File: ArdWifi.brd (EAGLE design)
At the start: 17.8 x 33 mm, 17 parts, among them Q1 8/16/20MHz, U1 ATMEGA328, U2 MIC5205

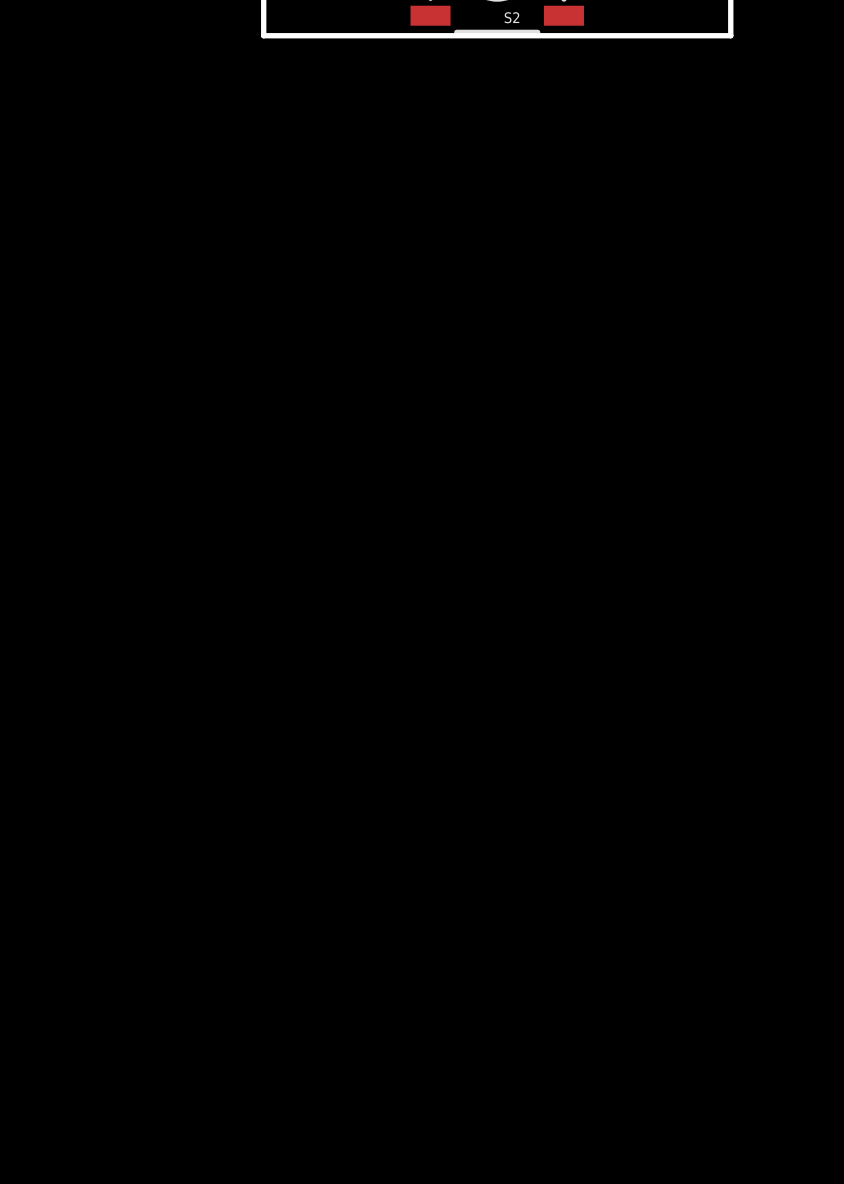
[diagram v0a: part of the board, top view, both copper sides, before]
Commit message: add wifi chip
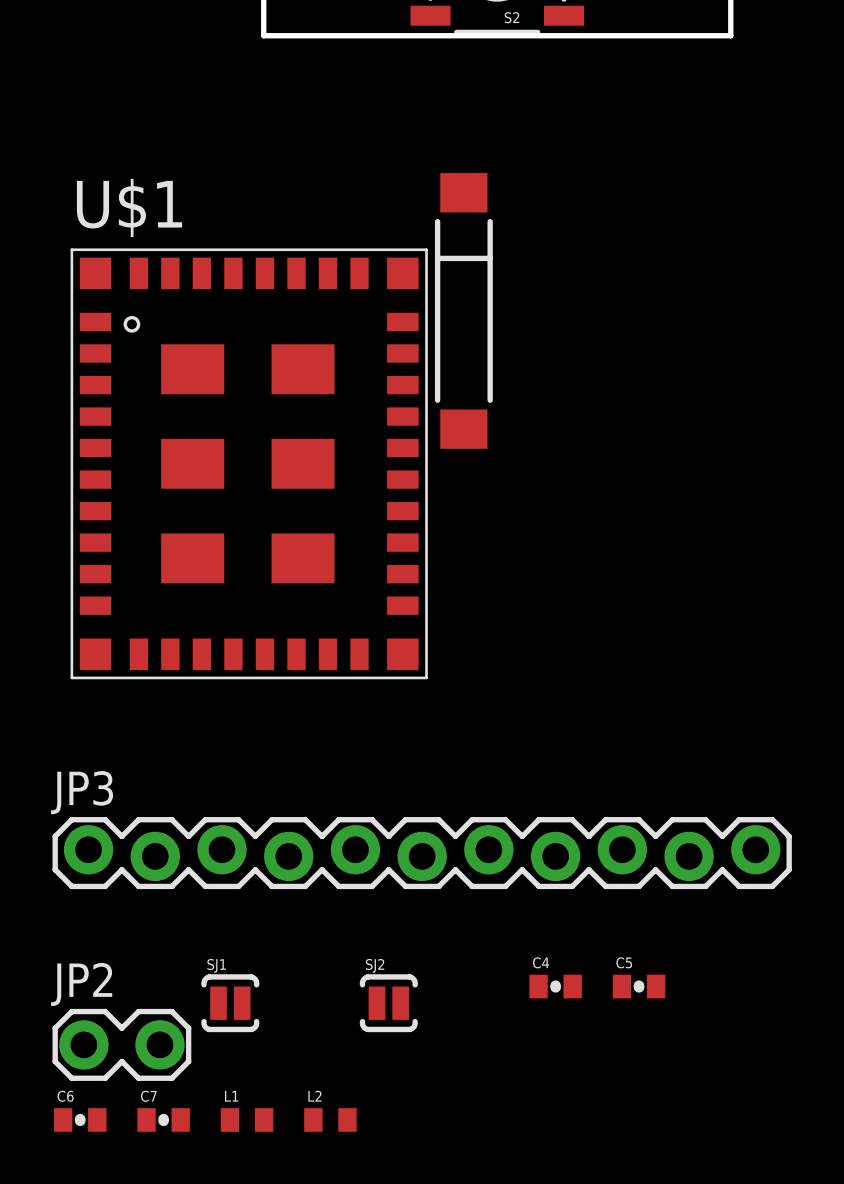
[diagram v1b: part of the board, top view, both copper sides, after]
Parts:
- added C4, C5: 1uF, SparkFun:0402-CAP
- added C6: 10pF, SparkFun:0402-CAP
- added C7: 2.2pF, SparkFun:0402-CAP
- added JP2: (no value), SparkFun:1X02_LOCK
- added JP3: M11LOCK, SparkFun:1X11_LOCK
- added L1: NL, SparkFun:C0402
- added L2: 2.2nH, SparkFun:C0402
- added SJ1, SJ2: SOLDERJUMPERNO, SparkFun:SJ_2S-NO
- added U$1: CC3000, centerblack_engineering:CC3000
- added U$3: ANTENNA2SMD2, SparkFun:ANTENNA-CHIP3
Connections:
- new net 3.3V: C5.2, JP3.11, U$1.P$19
- new net N$10: C6.1, C7.2, L2.2
- new net N$13: C6.2, U$1.P$35
- new net N$14: SJ1.1, U$1.P$30
- new net N$15: C7.1, L1.2, U$3.FEED
- new net N$16: SJ1.2, U$1.P$29
- new net N$17: SJ2.2, U$1.P$28
- new net N$18: SJ2.1, U$1.P$27
- new net SPI_CLK: JP3.7, U$1.P$17
- new net SPI_CS: JP3.3, U$1.P$12
- new net SPI_DIN: JP3.6, U$1.P$15
- new net SPI_DOUT: JP3.4, U$1.P$13
- new net SPI_IRQ: JP3.5, U$1.P$14
- new net VBAT_SW_EN: JP3.9, U$1.P$26
- new net VIO_HOST: C4.2, JP3.8, U$1.P$23
- new net WL_EN1: JP2.1, U$1.P$7
- new net WL_EN2: JP2.2, U$1.P$5
- new net WL_RS232_RX: JP3.2, U$1.P$8
- new net WL_RS232_TX: JP3.1, U$1.P$6
- net GND: now also C4.1, C5.1, JP3.10, L1.1, L2.1, U$1.P$1, U$1.P$10, U$1.P$11, U$1.P$16, U$1.P$18, U$1.P$20, U$1.P$21, U$1.P$22, U$1.P$25, U$1.P$31, U$1.P$32, U$1.P$33, U$1.P$34, U$1.P$36, U$1.P$37, U$1.P$38, U$1.P$39, U$1.P$40, U$1.P$41, U$1.P$42, U$1.P$43, U$1.P$44, U$1.P$45, U$1.P$46, U$1.P$9

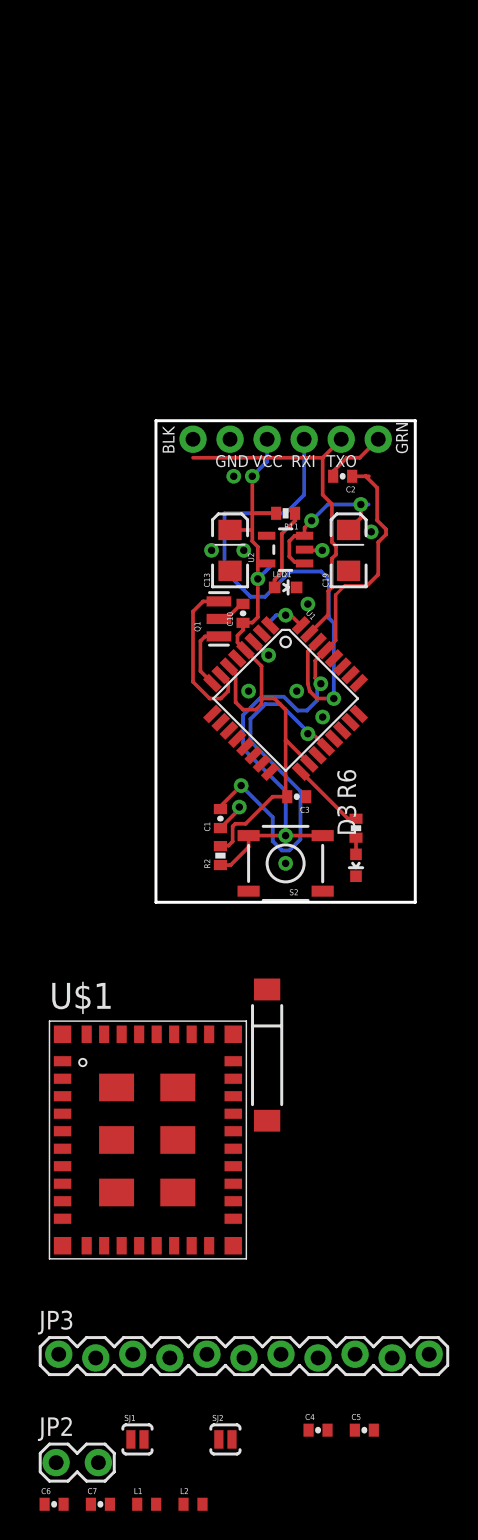
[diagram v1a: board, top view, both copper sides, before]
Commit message: connect wifi chip
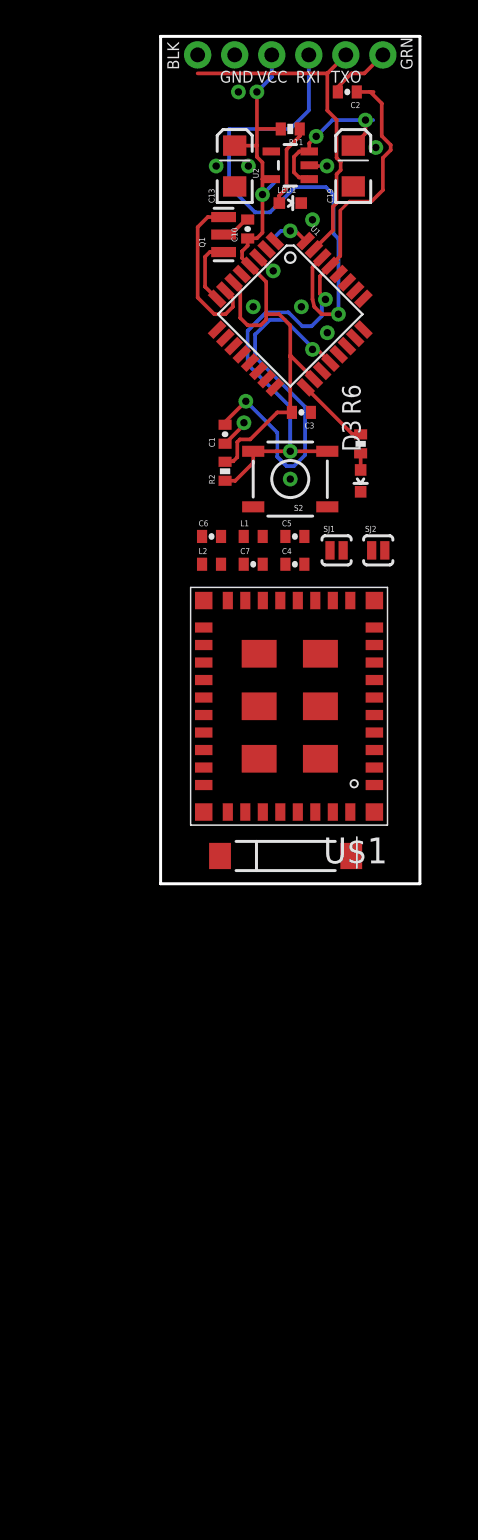
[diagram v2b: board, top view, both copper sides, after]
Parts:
- removed JP2: (no value), SparkFun:1X02_LOCK
- removed JP3: M11LOCK, SparkFun:1X11_LOCK
- moved C6 67.2 mm to (3.81, 25.1)
- moved L1 66.8 mm to (6.67, 25.1)
- moved C7 65.3 mm to (6.67, 23.2)
- moved L2 64.5 mm to (3.81, 23.2)
- moved SJ1 62.5 mm to (12.4, 24.1)
- moved SJ2 61.9 mm to (15.2, 24.1)
- moved C5 61.5 mm to (9.53, 25.1)
- moved C4 59.4 mm to (9.53, 23.2)
- moved U$1 51.5 mm to (15.9, 21.6), turned to 180 degrees
- moved C13 26.4 mm to (5.40, 50.5)
- moved C19 26.4 mm to (13.5, 50.5)
- moved C3 26.4 mm to (9.97, 33.6)
- moved LED1 26.4 mm to (9.21, 47.9)
- moved C1 26.4 mm to (4.74, 32.1)
- moved C2 26.4 mm to (13.1, 55.6)
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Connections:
- removed net 3.3V: C5.2, JP3.11, U$1.P$19
- removed net D10: U1.14
- removed net D3: U1.1
- removed net D5: U1.9
- removed net MISO: U1.16
- removed net MOSI: U1.15
- removed net SCK: R6.1, U1.17
- removed net WL_EN1: JP2.1, U$1.P$7
- net GND: no longer JP3.10
- net SPI_CLK: now also R6.1, U1.17; no longer JP3.7
- net SPI_CS: now also U1.14; no longer JP3.3
- net SPI_DIN: now also U1.15; no longer JP3.6
- net SPI_DOUT: now also U1.16; no longer JP3.4
- net SPI_IRQ: now also U1.1; no longer JP3.5
- net VBAT_SW_EN: now also U1.9; no longer JP3.9
- net VCC: now also C5.2, U$1.P$19
- net VIO_HOST: no longer JP3.8
- net WL_EN2: now also U$1.P$7; no longer JP2.2
- net WL_RS232_RX: no longer JP3.2
- net WL_RS232_TX: no longer JP3.1
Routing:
- net SCK: track 5.11 -> 0.00 mm
- net SPI_CLK: track 0.00 -> 5.11 mm
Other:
- board size 17.8 x 33 mm -> 17.8 x 58.1 mm

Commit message: added lvl shifter
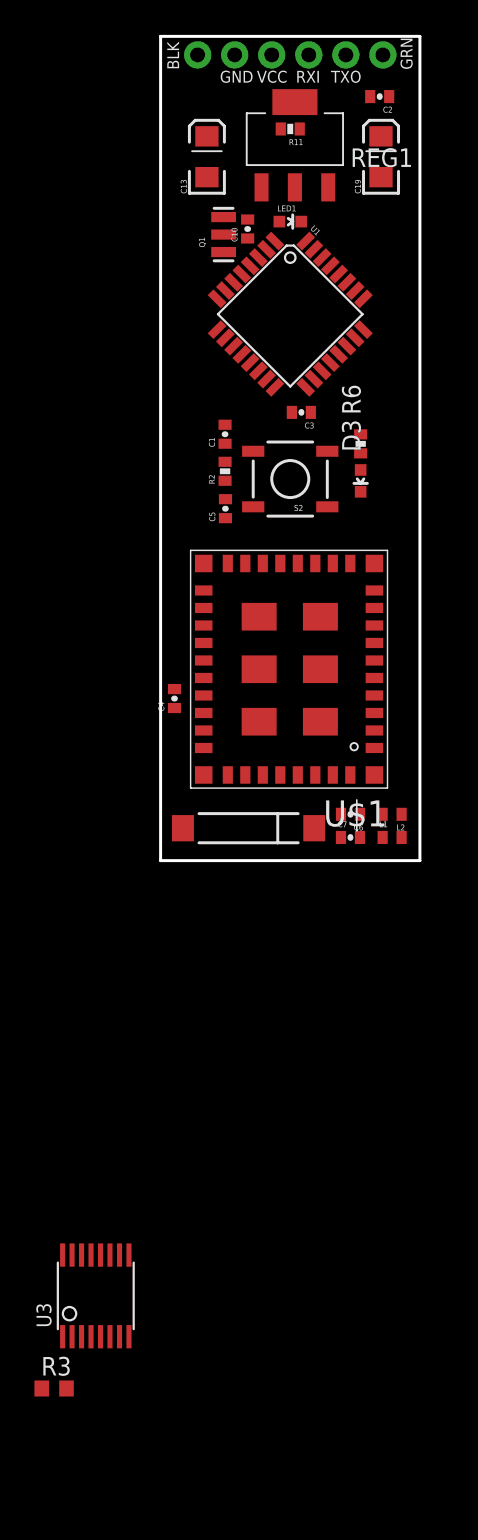
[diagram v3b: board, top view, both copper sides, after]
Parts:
- removed FRM1: (no value), Frames:LETTER
- removed SJ1, SJ2: SOLDERJUMPERNO, SparkFun:SJ_2S-NO
- removed U2: MIC5205, SparkFun:SOT23-5
- added R3: 10K, resistor:R0603
- added REG1: LDO_UA78M33, carrilib:SOT223
- added U3: TXB0106, McLEng:TSSOP16
- moved L1 22.7 mm to (16.2, 4.45)
- moved C6 21.3 mm to (13.3, 6.03), turned to 180 degrees
- moved L2 21.1 mm to (16.2, 6.03), turned to 180 degrees
- moved C7 19.9 mm to (13.3, 4.45)
- moved C4 12.4 mm to (1.27, 14.0), turned to 90 degrees
- moved C5 5.13 mm to (4.76, 27.0), turned to 90 degrees
- moved U$3 3.18 mm to (6.35, 5.08), turned to 270 degrees
- moved U$1 2.54 mm to (15.9, 24.1)
- moved C2 2.25 mm to (15.3, 55.2)
- moved C19 2.01 mm to (15.4, 51.1)
- moved C13 2.01 mm to (3.49, 51.1)
- moved LED1 1.27 mm to (9.21, 46.7)
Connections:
- removed net N$14: SJ1.1, U$1.P$30
- removed net N$17: SJ2.2, U$1.P$28
- new net +3V3: R3.1, U3.2
- new net N$114: R3.2, U3.8
- net GND: now also REG1.2, REG1.4, U3.9; no longer U2.2
- net N$16: now also U$1.P$30; no longer SJ1.2
- net N$18: now also U$1.P$28; no longer SJ2.1
- net RAW: now also JP1.4, REG1.1; no longer U2.1, U2.3
- net VCC: now also REG1.3, U3.15; no longer JP1.4, U2.5
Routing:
- net VCC: track 48.0 -> 0.00 mm, vias 2 -> 0
- net RESET: track 44.4 -> 0.00 mm, vias 2 -> 0
- net RXI: track 36.4 -> 0.00 mm, vias 1 -> 0
- net AREF: track 25.9 -> 0.00 mm, vias 2 -> 0
- net TXO: track 23.9 -> 0.00 mm
- net N$2: track 11.3 -> 0.00 mm
- net RAW: track 11.2 -> 0.00 mm, vias 2 -> 0
- net GND: track 6.59 -> 0.00 mm, vias 12 -> 0
- net N$38: track 5.68 -> 0.00 mm
- net SPI_CLK: track 5.11 -> 0.00 mm
- net N$1: track 4.63 -> 0.00 mm
- net DTR: track 4.34 -> 0.00 mm
- net D2: track 2.88 -> 0.00 mm, vias 1 -> 0
- net N$7: track 1.14 -> 0.00 mm
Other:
- board size 17.8 x 58.1 mm -> 17.8 x 56.5 mm
